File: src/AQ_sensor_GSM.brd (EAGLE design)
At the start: 110.2 x 66.3 mm, 177 parts, among them J1 F-1X03-SIP-100-32, J2 53261-0871, J4 S8411-45R, Q2 MMBT2222, Q3 MMBT2222, Q4 MMBT2222, Q5 MMBT2222, Q6 MMBT2222, Q7 MMBT2222, Q8 FS8205, T1 S8050, T2 S8050, U1 CP2102N-A02-GQFN28, U2 DS1307Z, U3 TP4056, U4 TPS63802DLAR, U5 TXS0108EPWR, U6 TPS63802DLAR, X1 ESP32-S3-WROOM-1-N16R8, Y1 32.768kHz

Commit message: Routing in Progress
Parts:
- removed 5V_IN1, 5V_IN2: ORANGE, led:CHIP-LED0603
- removed R40: 10K, rcl:R0603
- removed USB: (no value), led:CHIP-LED0603
- added 3.3IND: (no value), led:CHIP-LED0603
- added C37, C38: 0.1uF, rcl:C0603
- added CHRG, FULL: ORANGE, led:CHIP-LED0603
- added L4: 784778010, Fixed Inductors:784778010
- added POWER: 10118192-0001LF, AQ_sensor_GSM:AMPHENOL_10118192-0001LF
- added R62: 100k, SparkFun-Resistors:0603
- added R63: 432k, SparkFun-Resistors:0603
- added R64: 47k, SparkFun-Resistors:0603
- added R65: 1k, SparkFun-Resistors:0603
- added R66, R67: 10K, rcl:R0603
- added U7: TPS63802DLAR, TPS63802DLAR:VREG_TPS63802DLAR
- C21: device SparkFun-Capacitors:0402-TIGHT -> rcl:C0603
- C26: value 22pF -> TAJB106K016RNJ; device SparkFun-Capacitors:0402-TIGHT -> Resistor_Capacitor:CAP_TANT_B
- C28: value TAJB106K016RNJ -> 22pF; device Resistor_Capacitor:CAP_TANT_B -> rcl:C0603
- C32: value 0.1uF -> TAJB106K016RNJ; device rcl:C0603 -> Resistor_Capacitor:CAP_TANT_B
- moved D11 67.8 mm to (68.3, -0.88), flipped to the bottom
- moved C14 60.3 mm to (82.1, 37.7), turned to 270 degrees
- moved D4 53.3 mm to (56.0, 8.07), turned to 90 degrees
- moved D9 51.8 mm to (60.3, 8.03)
- moved R22 51.0 mm to (73.3, 8.19), turned to 180 degrees
- moved D8 50.8 mm to (58.1, 8.06)
- moved C33 49.2 mm to (65.2, 31.3), flipped to the bottom
- moved R2 47.0 mm to (38.0, 54.4)
- moved R46 46.4 mm to (59.3, 30.4), flipped to the bottom, turned to 90 degrees
- moved C34 44.6 mm to (62.9, 31.3), flipped to the bottom
- moved R21 43.9 mm to (76.3, 11.5), turned to 270 degrees
- moved R47 43.6 mm to (56.7, 30.4), flipped to the bottom, turned to 270 degrees
- moved Q3 43.3 mm to (73.2, 11.6), turned to 0 degrees
- moved R28 41.8 mm to (54.0, 20.4)
- moved 5V_IN 41.7 mm to (38.0, 59.2)
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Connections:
- removed net IO15: R40.1, X1.8
- removed net IO5: X1.5
- removed net IO6: X1.6
- removed net IO7: X1.7
- removed net IO8: X1.12
- removed net LBV: R10.2
- removed net L_MIS0: U$1.13, X1.38
- removed net L_MOSI: U$1.14, X1.39
- removed net L_SCK: U$1.12, X1.15
- removed net SD_CLK: MICRO_SD1.5, X1.31
- removed net SD_MISO: MICRO_SD1.3, X1.34
- removed net SD_MOSI: MICRO_SD1.7, X1.33
- new net IO21: X1.23
- new net IO35: X1.28
- new net IO36: X1.29
- new net IO37: X1.30
- new net IO38: X1.31
- new net IO40: X1.33
- new net IO41: X1.34
- new net IO42: X1.35
- new net IO45: R66.1, X1.26
- new net IO46: R67.1, X1.16
- new net MISO: MICRO_SD1.3, U$1.13, X1.38
- new net MOSI: MICRO_SD1.7, U$1.14, X1.39
- new net N$149: L4.2, U7.9
- new net N$150: L4.1, U7.7
- new net N$151: R62.1, U7.5
- new net N$152: R63.2, R64.1, U7.4
- new net SPI_CLK: MICRO_SD1.5, U$1.12, X1.15
- net 12V-IN: now also C26.1, C28.1, C37.1, R62.2, R65.2, U7.10; no longer C21.1
- net 4.0V_OUT: now also C10.1, C11.1, C12.1, C13.2, C14.2, C2.1, C5.2, C6.1, C9.1, D2.1, EC200_GSM.57, EC200_GSM.58, EC200_GSM.59, EC200_GSM.60, MODE.A, MRI.A, NST.A, PST.A, R502.2
- net BOOST_EN: now also R65.1, U7.1
- net DHT_LED: no longer X1.30
- net DHT_OUT: now also X1.7; no longer X1.29
- net GND: now also 3.3IND.C, C37.2, C38.2, POWER.4, POWER.5, POWER.SH1, POWER.SH2, POWER.SH3, POWER.SH4, POWER.SH5, POWER.SH6, R64.2, R66.2, R67.2, U7.2, U7.3, U7.8; no longer R40.2, USB.C
- net GSM_RST_O: now also X1.8; no longer X1.35
- net L_NSS: now also X1.12; no longer X1.16
- net N$138: no longer C28.1, C32.1
- net N$143: now also FULL.A; no longer 5V_IN1.A
- net N$145: now also CHRG.A; no longer 5V_IN2.A
- net N$146: now also FULL.C; no longer 5V_IN1.C
- net N$147: now also CHRG.C; no longer 5V_IN2.C
- net N$38: now also 3.3IND.A; no longer USB.A
- net PMS_LED: no longer X1.28
- net PMS_RX: now also X1.5; no longer X1.23
- net PMS_TX: now also X1.6; no longer X1.26
- net VUSB: now also C21.1, C32.1, C38.1, POWER.1, R63.1, U7.6; no longer C26.1
- net V_LIPO: now also R10.2; no longer C10.1, C11.1, C12.1, C13.2, C14.2, C2.1, C5.2, C6.1, C9.1, D2.1, EC200_GSM.57, EC200_GSM.58, EC200_GSM.59, EC200_GSM.60, MODE.A, MRI.A, NST.A, PST.A, R502.2
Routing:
- net VUSB: track 0.00 -> 173.8 mm, vias 0 -> 3
- net 5V_OUT: track 0.00 -> 89.5 mm, vias 0 -> 2
- net EUSB_N: track 0.00 -> 85.6 mm, vias 0 -> 1
- net USIM_VDD: track 0.00 -> 83.7 mm, vias 0 -> 2
- net SIMRST: track 0.00 -> 78.8 mm, vias 0 -> 2
- net EUSB_P: track 0.00 -> 78.0 mm, vias 0 -> 2
- net SIMCLK: track 0.00 -> 77.0 mm, vias 0 -> 2
- net SIMDATA: track 0.00 -> 75.3 mm, vias 0 -> 2
- net L_NSS: track 0.00 -> 68.8 mm, vias 0 -> 2
- net BOOST_EN: track 0.00 -> 66.9 mm, vias 0 -> 2
- net G_USB_VBUS: track 0.00 -> 57.7 mm, vias 0 -> 3
- net EUART_N: track 0.00 -> 53.9 mm, vias 0 -> 3
- net EUART_P: track 0.00 -> 51.5 mm, vias 0 -> 3
- net G_USB_N: track 0.00 -> 42.9 mm, vias 0 -> 2
- net G_USB_P: track 0.00 -> 42.9 mm, vias 0 -> 2
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
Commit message: 90% routed
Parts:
- removed DHT: GREEN, led:CHIP-LED0603
- removed PMS: ORANGE, led:CHIP-LED0603
- removed R11, R49: 200, rcl:R0603
- removed R16, R4: 470R, rcl:R0603
- removed RXT, TXT: (no value), led:CHIP-LED0603
- moved D10 16.8 mm to (59.8, 11.6), turned to 0 degrees
- moved D11 7.06 mm to (62.1, 2.37)
- moved R7 5.02 mm to (78.6, 52.6)
- moved 3.3IND 4.86 mm to (75.8, 52.5)
- moved C23 4.58 mm to (34.0, 32.8)
- moved C24 4.58 mm to (35.2, 17.3)
- moved C7 4.58 mm to (34.1, 29.5)
- moved L3 4.58 mm to (42.5, 24.9)
- moved R17 4.58 mm to (29.9, 21.9)
- moved U4 4.58 mm to (34.7, 24.6)
- moved R19 4.58 mm to (30.0, 23.6)
- moved R20 4.58 mm to (30.0, 25.4)
- moved R59 4.58 mm to (29.9, 27.0)
- moved C22 4.58 mm to (35.1, 20.5)
- moved R67 3.78 mm to (86.2, 33.2)
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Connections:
- removed net DHT_LED: R16.2
- removed net N$54 (its old number): R11.1, TXT.C
- removed net N$55 (its old number): R49.1, RXT.C
- removed net N$56 (its old number): TXT.A, U1.19
- removed net N$57 (its old number): RXT.A, U1.18
- removed net PMS_LED: R4.2
- net +3V3: no longer R11.2, R49.2
- net GND: no longer DHT.C, PMS.C, RST2.S1, RST2.S2
- net N$27: now also U1.18; no longer DHT.A, R16.1
- net N$4: now also U1.19; no longer PMS.A, R4.1
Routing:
- net ESP_RST: track 6.93 -> 193.8 mm, vias 0 -> 4
- net +3V3: track 14.5 -> 188.4 mm, vias 0 -> 8
- net GND: track 10.5 -> 171.0 mm, vias 47 -> 44
- net DHT_OUT: track 3.39 -> 136.9 mm, vias 0 -> 4
- net 4.0V_OUT: track 36.6 -> 169.2 mm, vias 0 -> 6
- net 5V_OUT: track 89.5 -> 219.8 mm, vias 2 -> 6
- net VUSB: track 173.8 -> 278.8 mm, vias 3 -> 6
- net DTR: track 2.30 -> 107.1 mm, vias 0 -> 3
- net V_LIPO: track 23.1 -> 111.6 mm, vias 3 -> 6
- net RTS: track 2.66 -> 84.7 mm, vias 0 -> 2
- net BMSV: track 2.02 -> 78.8 mm, vias 0 -> 1
- net USIM_GND: track 0.00 -> 76.8 mm, vias 0 -> 2
- net VDD_EXT: track 7.77 -> 68.6 mm, vias 0 -> 4
- net GSM_RST_O: track 0.00 -> 57.3 mm, vias 0 -> 2
- net N$34: track 0.00 -> 55.7 mm, vias 0 -> 2
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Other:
- board size 110.2 x 66.3 mm -> 9.2 x 5.7 mm

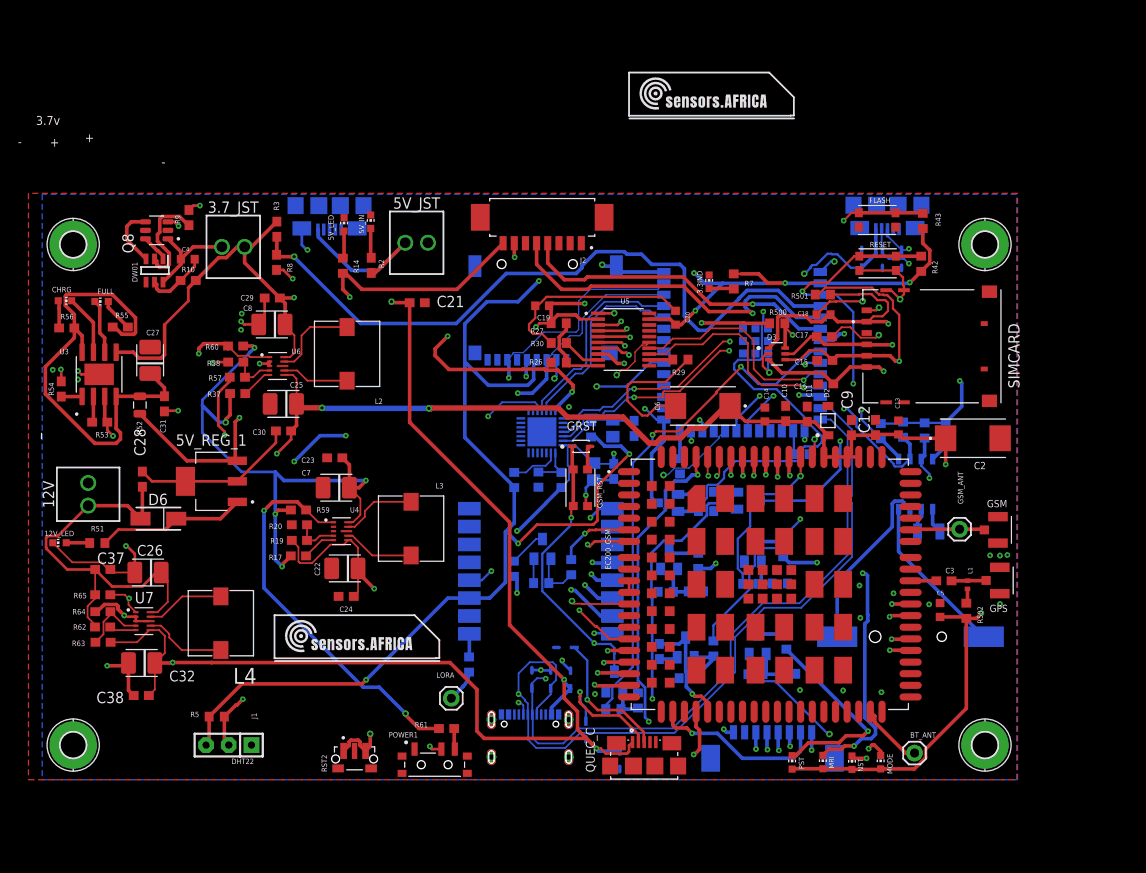
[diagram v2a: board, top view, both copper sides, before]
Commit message: 100% routed Minus Board Outline
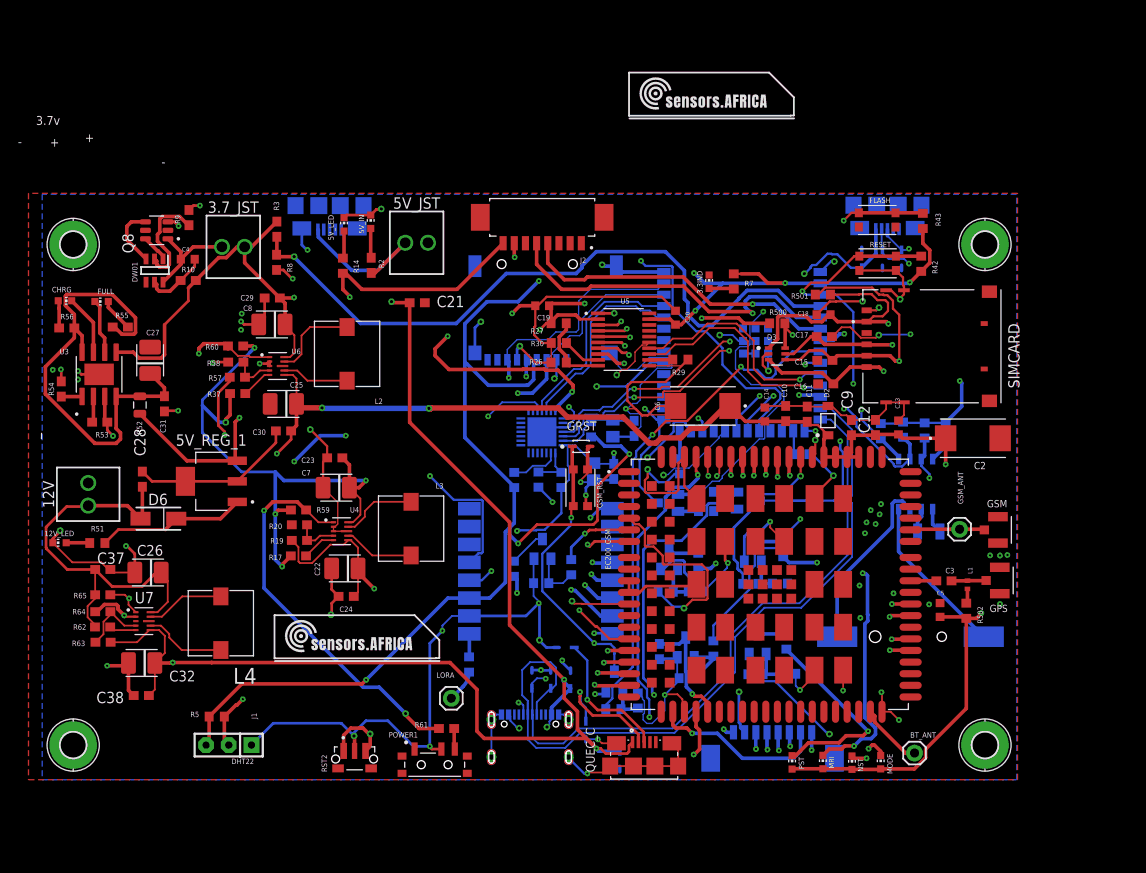
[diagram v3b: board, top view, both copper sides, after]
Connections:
- removed net IO11: X1.19
- removed net N$128: U$1.5
- removed net N$140: JTAG.A1_B12, JTAG.B1_A12, JTAG.SH1, JTAG.SH2, JTAG.SH3, JTAG.SH4
- new net DIO0: U$1.5, X1.19
- net GND: now also JTAG.A1_B12, JTAG.B1_A12, JTAG.SH1, JTAG.SH2, JTAG.SH3, JTAG.SH4
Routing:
- net GND: track 171.0 -> 471.9 mm, vias 44 -> 75
- net DIO0: track 0.00 -> 100.2 mm, vias 0 -> 2
- net NET_MODE: track 0.00 -> 22.7 mm, vias 0 -> 1
- net RTC_SQW: track 37.6 -> 51.5 mm
- net DTR: track 107.1 -> 97.9 mm
- net VUSB: track 278.8 -> 285.8 mm, vias 6 -> 8
- net 5V_OUT: track 219.8 -> 224.1 mm
- net ESP_RST: track 193.8 -> 197.1 mm
- net RTS: track 84.7 -> 86.2 mm
- net SPI_CLK: track 61.9 -> 63.3 mm
- net USIM_DET: track 54.7 -> 56.0 mm
- net IO0: track 56.6 -> 57.7 mm
- net BMSV: track 78.8 -> 78.0 mm
- net MCU_DTR: track 28.2 -> 29.0 mm
- net 12V-IN: track 46.1 -> 46.8 mm
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
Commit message: Resolved multiple shared output pins
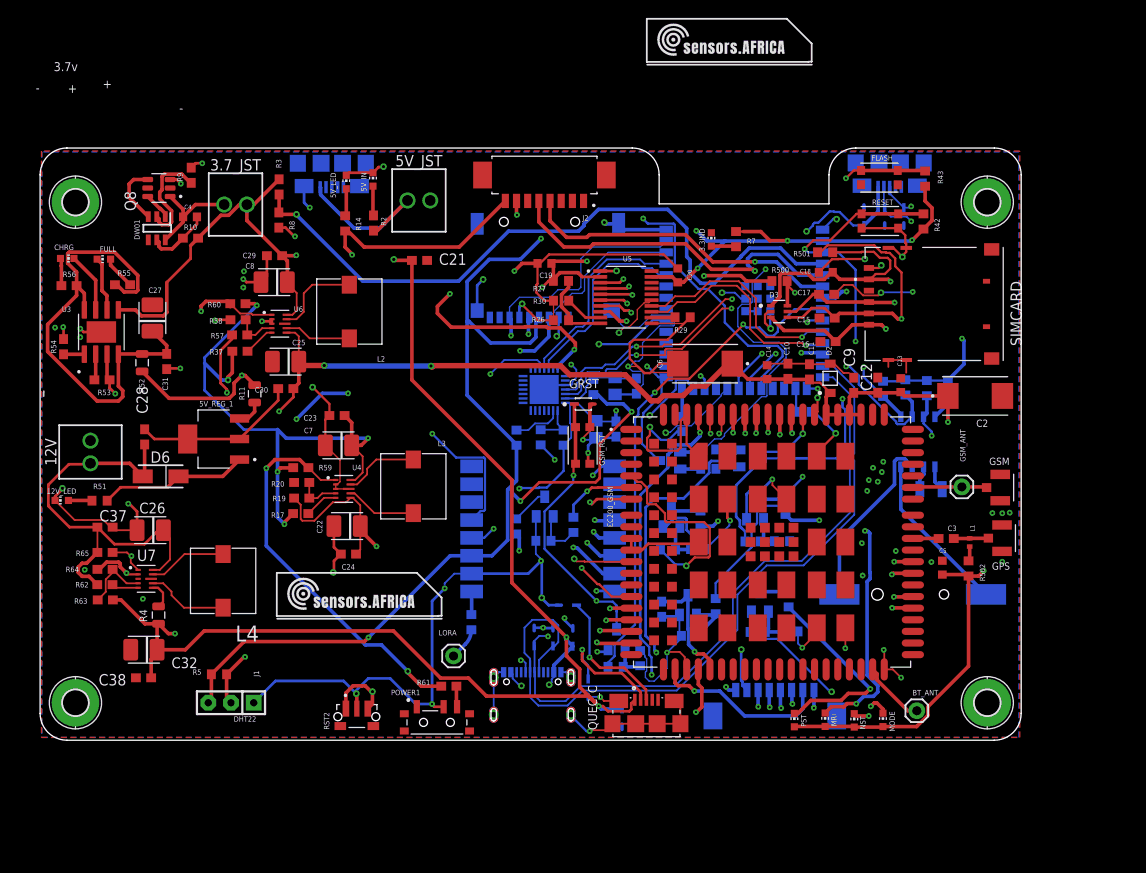
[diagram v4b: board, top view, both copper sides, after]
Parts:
- added R11, R4: 0.4R, Resistor_Capacitor:RES_0805
- moved C12 4.74 mm to (94.7, 41.0)
- moved C18 4.74 mm to (88.9, 53.6)
- moved CHRG 4.74 mm to (4.03, 55.1)
- moved GRST 4.74 mm to (61.8, 38.9)
- moved J2 4.74 mm to (57.4, 64.5)
- moved MICRO_SD1 4.74 mm to (57.9, 55.7)
- moved R501 4.74 mm to (88.8, 55.8)
- moved R9 4.74 mm to (17.9, 64.5)
- moved C28 4.74 mm to (12.7, 35.2)
- moved C3 4.74 mm to (102.4, 23.8)
- moved EC200_GSM 4.74 mm to (82.9, 23.4)
- moved GSM_RST 4.74 mm to (61.7, 34.2)
- moved Q4 4.74 mm to (71.6, 26.3)
- moved R13 4.74 mm to (57.3, 23.6)
- moved R24 4.74 mm to (74.6, 22.6)
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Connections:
- new net N$115: R4.2, U7.6
- new net N$116: 5V_REG_1.3, R11.2
- net VUSB: now also R11.1, R4.1; no longer 5V_REG_1.3, U7.6
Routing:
- net GND: track 471.9 -> 460.1 mm, vias 75 -> 76
- net VUSB: track 285.8 -> 282.3 mm
- net N$115: track 0.00 -> 3.10 mm
- net N$116: track 0.00 -> 3.03 mm
- net 12V-IN: track 46.8 -> 49.3 mm
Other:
- board size 9.2 x 5.7 mm -> 109.8 x 66.2 mm

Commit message: Route PCB 100%
Add 5V buck boost converter for charging Side

Add boost converter for 4.0V voltage rail

Add 5V Boost converter for the 5V rail

Add 3.3V LDO to power MCU
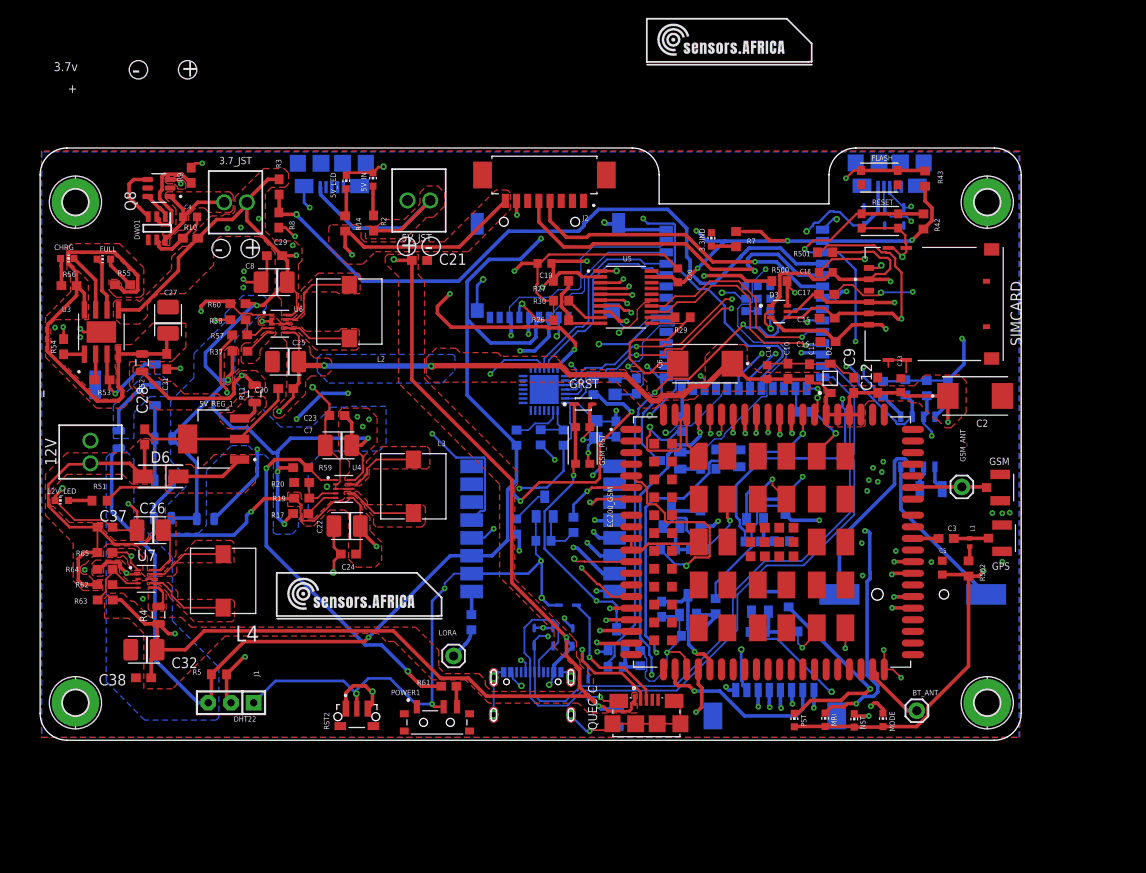
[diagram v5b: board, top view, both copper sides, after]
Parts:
- added JUMP4V, JUMP5V, JUMPVL, R16, R40: 0.4R, Resistor_Capacitor:RES_0805
- added U8: AMS1117-3.3, AMS1117-3.3:SOT229P700X180-4N
- LORA: value (none) -> NA
- moved C27 1.77 mm to (15.3, 48.2)
- moved 3.7_JST 0.25 mm to (22.9, 61.4)
- turned 5V_JST to 180 degrees
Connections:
- net G_GPIO1 renamed N$128
- new net N$117: JUMPVL.1, R40.1, U8.3
- new net N$118: R16.2, U8.2
- new net N$140: J2.1
- new net N$153: J2.2
- new net N$154: J2.3
- new net N$155: J2.6
- net +3V3: now also R16.1
- net 4.0V_OUT: now also JUMP4V.1
- net 5V_OUT: now also JUMP5V.1, R40.2
- net GND: now also U8.1
- net V_LIPO: now also JUMP4V.2, JUMP5V.2, JUMPVL.2
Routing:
- net +3V3: track 188.4 -> 222.3 mm
- net 5V_OUT: track 224.1 -> 248.6 mm, vias 6 -> 7
- net V_LIPO: track 111.6 -> 132.2 mm, vias 6 -> 13
- net 4.0V_OUT: track 169.2 -> 184.2 mm, vias 6 -> 7
- net VUSB: track 282.3 -> 292.4 mm
- net N$117: track 0.00 -> 8.42 mm
- net N$118: track 0.00 -> 7.53 mm
- net GND: track 460.1 -> 467.3 mm, vias 76 -> 77
- net 12V-IN: track 49.3 -> 50.4 mm
- net N$138: track 53.9 -> 53.0 mm
- added copper zone on layer 16, net +3V3
- added copper zone on layer 1, net 12V-IN
- added copper zone on layer 1, net 4.0V_OUT
- added copper zone on layer 16, net 4.0V_OUT
- added copper zone on layer 1, net 5V_OUT
- added copper zone on layer 15, net 5V_OUT
- added copper zone on layer 2, net 5V_OUT
- added copper zone on layer 1, net BATT-
- added copper zone on layer 1, net BOOST_EN
- added copper zone on layer 1, net N$115
- added copper zone on layer 1, net N$116
- added copper zone on layer 16, net N$118
- added copper zone on layer 1, net N$13
- added copper zone on layer 1, net N$138
- added copper zone on layer 1, net N$14
- added copper zone on layer 1, net N$149
- added copper zone on layer 1, net N$150
- added copper zone on layer 1, net N$17
- added copper zone on layer 1, net N$24
- added copper zone on layer 1, net N$36
- added copper zone on layer 1, net N$45
- added copper zone on layer 1, net VUSB
- added copper zone on layer 2, net VUSB
- added copper zone on layer 1, net V_LIPO
- added copper zone on layer 16, net V_LIPO
